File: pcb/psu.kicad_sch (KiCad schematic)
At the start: 35 parts

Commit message: add footprints
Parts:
- C201: renamed from C?; footprint (none) -> fpga:BGA256C100P16X16_1700X1700X155
- C202, C204, C205, C206, C207, C208, C209, C210, C211, C212, C213, C214, C215, C216, C217, C218, C219: renamed from C?; footprint (none) -> Capacitor_SMD:C_0805_2012Metric_Pad1.18x1.45mm_HandSolder
- C203: renamed from C?; footprint (none) -> Capacitor_SMD:C_1210_3225Metric_Pad1.33x2.70mm_HandSolder
- JP201, JP202, JP203: renamed from JP?; footprint (none) -> Jumper:SolderJumper-3_P1.3mm_Open_Pad1.0x1.5mm_NumberLabels
- L201, L202, L203: renamed from L?; footprint (none) -> Inductor_SMD:L_1210_3225Metric_Pad1.42x2.65mm_HandSolder
- R201, R202, R203, R204, R205, R206, R207, R208: renamed from R?; footprint (none) -> Resistor_SMD:R_0805_2012Metric_Pad1.20x1.40mm_HandSolder
- gave numbers to parts that had none: 2

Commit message: start layout
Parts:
- C201: footprint fpga:BGA256C100P16X16_1700X1700X155 -> Capacitor_SMD:C_0805_2012Metric_Pad1.18x1.45mm_HandSolder
- U201: footprint PWP14_2P31X2P46 -> TPS54325:TPS54325PWPR
- U202: footprint PWP16_2P31X2P46 -> TPS54294:TPS54294PWP
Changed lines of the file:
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@@
     (pin "2")
+  )
+  (symbol (lib_id "power:+1V8") (at 16.51 134.62 0) (unit 1)
+    (in_bom yes) (on_board yes) (fields_autoplaced)
+    (property "Reference" "#PWR0104" (id 0) (at 16.51 138.43 0)
+      (effects (font (size 1.27 1.27)) hide)
+    )
+    (property "Value" "+1V8" (id 1) (at 16.51 129.54 0))
+    (property "Footprint" "" (id 2) (at 16.51 134.62 0)
+      (effects (font (size 1.27 1.27)) hide)
+    )
+    (property "Datasheet" "" (id 3) (at 16.51 134.62 0)
+      (effects (font (size 1.27 1.27)) hide)
+    )
+    (pin "1")
   )
   (symbol (lib_id "Device:R") (at 195.58 146.05 0) (unit 1)
@@
       (effects (font (size 1.524 1.524)))
     )
-    (property "Footprint" "PWP16_2P31X2P46" (id 2) (at 154.94 115.824 0)
+    (property "Footprint" "TPS54294:TPS54294PWP" (id 2) (at 154.94 115.824 0)
       (effects (font (size 1.524 1.524)) hide)
     )
@@
     (pin "2")
   )
-  (symbol (lib_id "power:+1V8") (at 16.51 134.62 0) (unit 1)
-    (in_bom yes) (on_board yes) (fields_autoplaced)
-    (property "Reference" "#PWR0201" (id 0) (at 16.51 138.43 0)
-      (effects (font (size 1.27 1.27)) hide)
-    )
-    (property "Value" "+1V8" (id 1) (at 16.51 129.54 0))
-    (property "Footprint" "" (id 2) (at 16.51 134.62 0)
-      (effects (font (size 1.27 1.27)) hide)
-    )
-    (property "Datasheet" "" (id 3) (at 16.51 134.62 0)
-      (effects (font (size 1.27 1.27)) hide)
-    )
-    (pin "1")
-  )
   (symbol (lib_id "pspice:INDUCTOR") (at 71.12 134.62 0) (unit 1)
     (in_bom yes) (on_board yes)
@@
       (effects (font (size 1.524 1.524)))
     )
-    (property "Footprint" "PWP14_2P31X2P46" (id 2) (at 138.43 44.704 0)
+    (property "Footprint" "TPS54325:TPS54325PWPR" (id 2) (at 138.43 44.704 0)
       (effects (font (size 1.524 1.524)) hide)
     )
@@
       (effects (font (size 1.27 1.27)) (justify left))
     )
-    (property "Footprint" "fpga:BGA256C100P16X16_1700X1700X155" (id 2) (at 47.9552 147.32 0)
-      (effects (font (size 1.27 1.27)) hide)
-    )
+    (property "Footprint" "Capacitor_SMD:C_0805_2012Metric_Pad1.18x1.45mm_HandSolder" (id 2) (at 47.9552 147.32 0)
+      (effects (font (size 1.27 1.27)) hide)
+    )

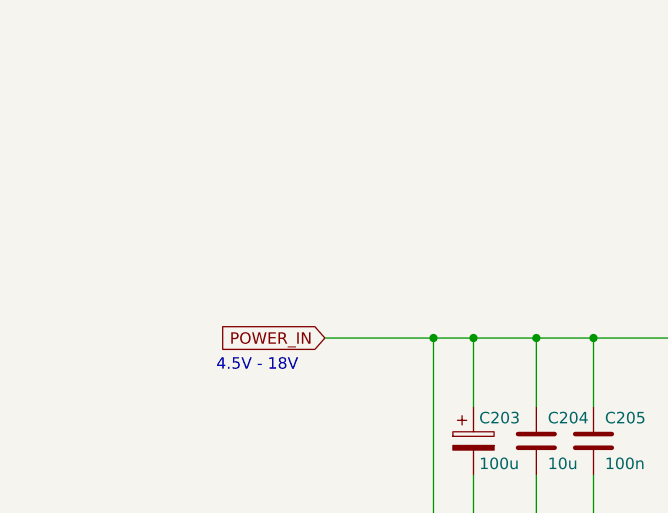
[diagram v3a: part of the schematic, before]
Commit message: add power input
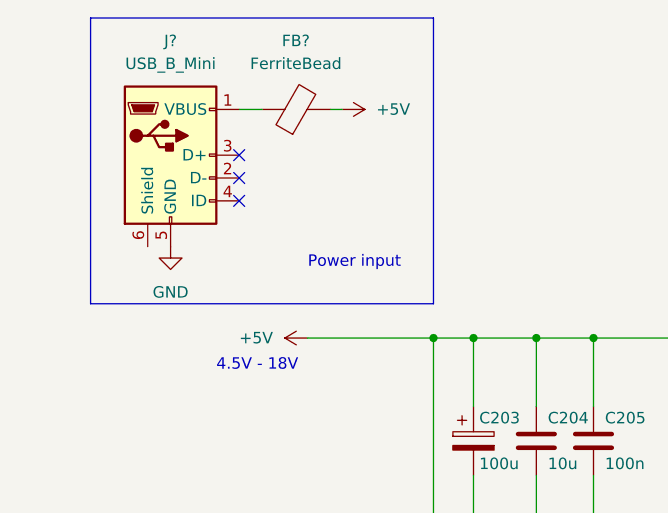
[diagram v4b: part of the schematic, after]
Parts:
- added FB?: FerriteBead, symbol Device:FerriteBead
- added J?: USB_B_Mini, symbol Connector:USB_B_Mini
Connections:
- net GND: now also J?.5 (GND)
- net POWER_IN renamed +5V
- net +5V: now also FB?.2
- new net: FB?.1, J?.1 (VBUS)
- no-connect marks 1 -> 4
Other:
- note added: "Power input"
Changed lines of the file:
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@@
   (junction (at 71.12 49.53) (diameter 0) (color 0 0 0 0)
   )
+  (no_connect (at 38.1 34.29))
   (no_connect (at 177.8 134.62))
+  (no_connect (at 38.1 31.75))
+  (no_connect (at 38.1 29.21))
   (wire (pts (xy 64.135 82.55) (xy 71.12 82.55))
     (stroke (width 0) (type default) (color 0 0 0 0))
@@
     (stroke (width 0) (type default) (color 0 0 0 0))
   )
+  (polyline (pts (xy 21.59 13.97) (xy 21.59 45.72))
+    (stroke (width 0) (type default) (color 0 0 0 0))
+  )
   (wire (pts (xy 180.34 132.08) (xy 180.34 153.67))
     (stroke (width 0) (type default) (color 0 0 0 0))
@@
     (stroke (width 0) (type default) (color 0 0 0 0))
   )
+  (polyline (pts (xy 21.59 13.97) (xy 59.69 13.97))
+    (stroke (width 0) (type default) (color 0 0 0 0))
+  )
   (wire (pts (xy 77.47 134.62) (xy 106.68 134.62))
     (stroke (width 0) (type default) (color 0 0 0 0))
@@
     (stroke (width 0) (type default) (color 0 0 0 0))
   )
+  (wire (pts (xy 38.1 24.13) (xy 40.64 24.13))
+    (stroke (width 0) (type default) (color 0 0 0 0))
+  )
   (wire (pts (xy 130.81 158.75) (xy 154.94 158.75))
     (stroke (width 0) (type default) (color 0 0 0 0))
@@
     (stroke (width 0) (type default) (color 0 0 0 0))
   )
-  (wire (pts (xy 47.625 49.53) (xy 59.69 49.53))
+  (wire (pts (xy 45.72 49.53) (xy 59.69 49.53))
     (stroke (width 0) (type default) (color 0 0 0 0))
   )
@@
     (stroke (width 0) (type default) (color 0 0 0 0))
   )
+  (polyline (pts (xy 59.69 13.97) (xy 59.69 45.72))
+    (stroke (width 0) (type default) (color 0 0 0 0))
+  )
+  (polyline (pts (xy 59.69 45.72) (xy 21.59 45.72))
+    (stroke (width 0) (type default) (color 0 0 0 0))
+  )
   (wire (pts (xy 106.68 133.35) (xy 106.68 134.62))
+    (stroke (width 0) (type default) (color 0 0 0 0))
+  )
+  (wire (pts (xy 48.26 24.13) (xy 49.53 24.13))
     (stroke (width 0) (type default) (color 0 0 0 0))
   )
@@
     (effects (font (size 1.27 1.27)) (justify left bottom))
   )
+  (text "Power input" (at 45.72 41.91 0)
+    (effects (font (size 1.27 1.27)) (justify left bottom))
+  )
   (text "1%\n" (at 92.71 73.66 90)
     (effects (font (size 1.27 1.27)) (justify left bottom))
@@
   (text "lp>2.8A, lrms>2.1A" (at 62.23 132.08 0)
     (effects (font (size 1.27 1.27)) (justify left bottom))
-  )
-  (global_label "POWER_IN" (shape input) (at 47.625 49.53 180) (fields_autoplaced)
-    (effects (font (size 1.27 1.27)) (justify right))
-    (property "Intersheet References" "${INTERSHEET_REFS}" (id 0) (at 35.8381 49.4506 0)
-      (effects (font (size 1.27 1.27)) (justify right) hide)
-    )
   )
   (symbol (lib_id "power:GND") (at 154.94 163.83 0) (unit 1)
@@
     (pin "2")
   )
+  (symbol (lib_id "Connector:USB_B_Mini") (at 30.48 29.21 0) (unit 1)
+    (in_bom yes) (on_board yes) (fields_autoplaced)
+    (property "Reference" "J?" (id 0) (at 30.48 16.51 0))
+    (property "Value" "USB_B_Mini" (id 1) (at 30.48 19.05 0))
+    (property "Footprint" "" (id 2) (at 34.29 30.48 0)
+      (effects (font (size 1.27 1.27)) hide)
+    )
+    (property "Datasheet" "~" (id 3) (at 34.29 30.48 0)
+      (effects (font (size 1.27 1.27)) hide)
+    )
+    (pin "1")
+    (pin "2")
+    (pin "3")
+    (pin "4")
+    (pin "5")
+    (pin "6")
+  )
   (symbol (lib_id "Device:R") (at 95.25 59.69 0) (unit 1)
     (in_bom yes) (on_board yes)
@@
     (pin "1")
     (pin "2")
+  )
+  (symbol (lib_id "power:GND") (at 30.48 39.37 0) (mirror y) (unit 1)
+    (in_bom yes) (on_board yes) (fields_autoplaced)
+    (property "Reference" "#PWR?" (id 0) (at 30.48 45.72 0)
+      (effects (font (size 1.27 1.27)) hide)
+    )
+    (property "Value" "GND" (id 1) (at 30.48 44.45 0))
+    (property "Footprint" "" (id 2) (at 30.48 39.37 0)
+      (effects (font (size 1.27 1.27)) hide)
+    )
+    (property "Datasheet" "" (id 3) (at 30.48 39.37 0)
+      (effects (font (size 1.27 1.27)) hide)
+    )
+    (pin "1")
   )
   (symbol (lib_id "Device:C") (at 193.04 129.54 0) (unit 1)
@@
     (pin "2")
   )
+  (symbol (lib_id "power:+5V") (at 49.53 24.13 270) (unit 1)
+    (in_bom yes) (on_board yes) (fields_autoplaced)
+    (property "Reference" "#PWR?" (id 0) (at 45.72 24.13 0)
+      (effects (font (size 1.27 1.27)) hide)
+    )
+    (property "Value" "+5V" (id 1) (at 53.34 24.1299 90)
+      (effects (font (size 1.27 1.27)) (justify left))
+    )
+    (property "Footprint" "" (id 2) (at 49.53 24.13 0)
+      (effects (font (size 1.27 1.27)) hide)
+    )
+    (property "Datasheet" "" (id 3) (at 49.53 24.13 0)
+      (effects (font (size 1.27 1.27)) hide)
+    )
+    (pin "1")
+  )
   (symbol (lib_id "Device:C") (at 214.63 124.46 0) (unit 1)
     (in_bom yes) (on_board yes) (fields_autoplaced)
@@
     )
     (property "Datasheet" "~" (id 3) (at 265.43 134.62 0)
+      (effects (font (size 1.27 1.27)) hide)
+    )
+    (pin "1")
+    (pin "2")
+  )
+  (symbol (lib_id "Device:FerriteBead") (at 44.45 24.13 90) (unit 1)
+    (in_bom yes) (on_board yes) (fields_autoplaced)
+    (property "Reference" "FB?" (id 0) (at 44.3992 16.51 90))
+    (property "Value" "FerriteBead" (id 1) (at 44.3992 19.05 90))
+    (property "Footprint" "" (id 2) (at 44.45 25.908 90)
+      (effects (font (size 1.27 1.27)) hide)
+    )
+    (property "Datasheet" "~" (id 3) (at 44.45 24.13 0)
       (effects (font (size 1.27 1.27)) hide)
     )
@@
     (pin "2")
   )
+  (symbol (lib_id "power:+5V") (at 45.72 49.53 90) (unit 1)
+    (in_bom yes) (on_board yes)
+    (property "Reference" "#PWR?" (id 0) (at 49.53 49.53 0)
+      (effects (font (size 1.27 1.27)) hide)
+    )
+    (property "Value" "+5V" (id 1) (at 38.1 49.53 90)
+      (effects (font (size 1.27 1.27)) (justify right))
+    )
+    (property "Footprint" "" (id 2) (at 45.72 49.53 0)
+      (effects (font (size 1.27 1.27)) hide)
+    )
+    (property "Datasheet" "" (id 3) (at 45.72 49.53 0)
+      (effects (font (size 1.27 1.27)) hide)
+    )
+    (pin "1")
+  )
   (symbol (lib_id "Device:C") (at 71.12 60.96 0) (unit 1)

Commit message: add footprint to usb
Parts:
- J?: footprint (none) -> usb:USB2066-05-RBHM-15-STB-00-00-A
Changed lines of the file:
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@@
   (no_connect (at 38.1 34.29))
   (no_connect (at 177.8 134.62))
+  (no_connect (at 38.1 29.21))
   (no_connect (at 38.1 31.75))
-  (no_connect (at 38.1 29.21))
   (wire (pts (xy 64.135 82.55) (xy 71.12 82.55))
     (stroke (width 0) (type default) (color 0 0 0 0))
@@
     (property "Reference" "J?" (id 0) (at 30.48 16.51 0))
     (property "Value" "USB_B_Mini" (id 1) (at 30.48 19.05 0))
-    (property "Footprint" "" (id 2) (at 34.29 30.48 0)
-      (effects (font (size 1.27 1.27)) hide)
-    )
+    (property "Footprint" "usb:USB2066-05-RBHM-15-STB-00-00-A" (id 2) (at 34.29 30.48 0)
+      (effects (font (size 1.27 1.27)) hide)
+    )

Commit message: change footprint of debug_connector
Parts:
- J201: renamed from J?; footprint usb:USB2066-05-RBHM-15-STB-00-00-A -> (none)
- gave numbers to parts that had none: 1
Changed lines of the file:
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@@
   (no_connect (at 38.1 34.29))
   (no_connect (at 177.8 134.62))
+  (no_connect (at 38.1 31.75))
   (no_connect (at 38.1 29.21))
-  (no_connect (at 38.1 31.75))
   (wire (pts (xy 64.135 82.55) (xy 71.12 82.55))
     (stroke (width 0) (type default) (color 0 0 0 0))
@@
   (symbol (lib_id "Connector:USB_B_Mini") (at 30.48 29.21 0) (unit 1)
     (in_bom yes) (on_board yes) (fields_autoplaced)
-    (property "Reference" "J?" (id 0) (at 30.48 16.51 0))
+    (property "Reference" "J201" (id 0) (at 30.48 16.51 0))
     (property "Value" "USB_B_Mini" (id 1) (at 30.48 19.05 0))
-    (property "Footprint" "usb:USB2066-05-RBHM-15-STB-00-00-A" (id 2) (at 34.29 30.48 0)
+    (property "Footprint" "" (id 2) (at 34.29 30.48 0)
       (effects (font (size 1.27 1.27)) hide)
     )
@@
   (symbol (lib_id "power:GND") (at 30.48 39.37 0) (mirror y) (unit 1)
     (in_bom yes) (on_board yes) (fields_autoplaced)
-    (property "Reference" "#PWR?" (id 0) (at 30.48 45.72 0)
+    (property "Reference" "#PWR0113" (id 0) (at 30.48 45.72 0)
       (effects (font (size 1.27 1.27)) hide)
     )
@@
   (symbol (lib_id "power:+5V") (at 49.53 24.13 270) (unit 1)
     (in_bom yes) (on_board yes) (fields_autoplaced)
-    (property "Reference" "#PWR?" (id 0) (at 45.72 24.13 0)
+    (property "Reference" "#PWR0112" (id 0) (at 45.72 24.13 0)
       (effects (font (size 1.27 1.27)) hide)
     )
@@
   (symbol (lib_id "Device:FerriteBead") (at 44.45 24.13 90) (unit 1)
     (in_bom yes) (on_board yes) (fields_autoplaced)
-    (property "Reference" "FB?" (id 0) (at 44.3992 16.51 90))
+    (property "Reference" "FB201" (id 0) (at 44.3992 16.51 90))
     (property "Value" "FerriteBead" (id 1) (at 44.3992 19.05 90))
     (property "Footprint" "" (id 2) (at 44.45 25.908 90)
@@
   (symbol (lib_id "power:+5V") (at 45.72 49.53 90) (unit 1)
     (in_bom yes) (on_board yes)
-    (property "Reference" "#PWR?" (id 0) (at 49.53 49.53 0)
-      (effects (font (size 1.27 1.27)) hide)
-    )
+    (property "Reference" "#PWR0111" (id 0) (at 49.53 49.53 0)
+      (effects (font (size 1.27 1.27)) hide)
+    )

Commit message: assign the last footprints
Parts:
- removed FB201: FerriteBead, symbol Device:FerriteBead
- J201: footprint (none) -> usb:USB2066-05-RBHM-15-STB-00-00-A
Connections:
- net +5V: now also J201.1 (VBUS)
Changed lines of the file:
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@@
-    (stroke (width 0) (type default) (color 0 0 0 0))
-  )
-  (wire (pts (xy 38.1 24.13) (xy 40.64 24.13))
     (stroke (width 0) (type default) (color 0 0 0 0))
   )
@@
   )
   (wire (pts (xy 106.68 133.35) (xy 106.68 134.62))
-    (stroke (width 0) (type default) (color 0 0 0 0))
-  )
-  (wire (pts (xy 48.26 24.13) (xy 49.53 24.13))
     (stroke (width 0) (type default) (color 0 0 0 0))
   )
@@
     (property "Reference" "J201" (id 0) (at 30.48 16.51 0))
     (property "Value" "USB_B_Mini" (id 1) (at 30.48 19.05 0))
-    (property "Footprint" "" (id 2) (at 34.29 30.48 0)
-      (effects (font (size 1.27 1.27)) hide)
-    )
+    (property "Footprint" "usb:USB2066-05-RBHM-15-STB-00-00-A" (id 2) (at 34.29 30.48 0))
     (property "Datasheet" "~" (id 3) (at 34.29 30.48 0)
       (effects (font (size 1.27 1.27)) hide)
@@
     (pin "2")
   )
-  (symbol (lib_id "power:+5V") (at 49.53 24.13 270) (unit 1)
-    (in_bom yes) (on_board yes) (fields_autoplaced)
-    (property "Reference" "#PWR0112" (id 0) (at 45.72 24.13 0)
-      (effects (font (size 1.27 1.27)) hide)
-    )
-    (property "Value" "+5V" (id 1) (at 53.34 24.1299 90)
-      (effects (font (size 1.27 1.27)) (justify left))
-    )
-    (property "Footprint" "" (id 2) (at 49.53 24.13 0)
-      (effects (font (size 1.27 1.27)) hide)
-    )
-    (property "Datasheet" "" (id 3) (at 49.53 24.13 0)
+  (symbol (lib_id "power:+5V") (at 38.1 24.13 270) (unit 1)
+    (in_bom yes) (on_board yes) (fields_autoplaced)
+    (property "Reference" "#PWR0112" (id 0) (at 34.29 24.13 0)
+      (effects (font (size 1.27 1.27)) hide)
+    )
+    (property "Value" "+5V" (id 1) (at 41.91 24.1299 90)
+      (effects (font (size 1.27 1.27)) (justify left))
+    )
+    (property "Footprint" "" (id 2) (at 38.1 24.13 0)
+      (effects (font (size 1.27 1.27)) hide)
+    )
+    (property "Datasheet" "" (id 3) (at 38.1 24.13 0)
       (effects (font (size 1.27 1.27)) hide)
     )
@@
       (effects (font (size 1.27 1.27)) hide)
     )
-    (pin "1")
-    (pin "2")
-  )
-  (symbol (lib_id "Device:FerriteBead") (at 44.45 24.13 90) (unit 1)
-    (in_bom yes) (on_board yes) (fields_autoplaced)
-    (property "Reference" "FB201" (id 0) (at 44.3992 16.51 90))
-    (property "Value" "FerriteBead" (id 1) (at 44.3992 19.05 90))
-    (property "Footprint" "" (id 2) (at 44.45 25.908 90)
-      (effects (font (size 1.27 1.27)) hide)
-    )
-    (property "Datasheet" "~" (id 3) (at 44.45 24.13 0)
-      (effects (font (size 1.27 1.27)) hide)
-    )

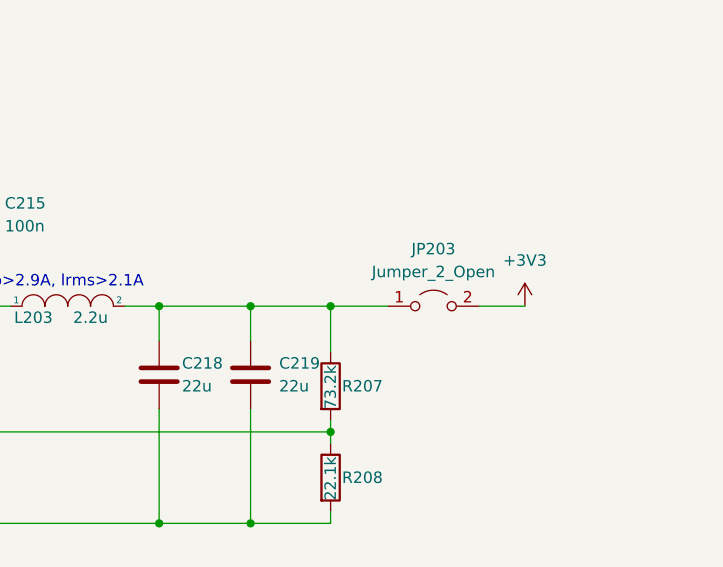
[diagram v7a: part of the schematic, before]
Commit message: psu wiring and power cables
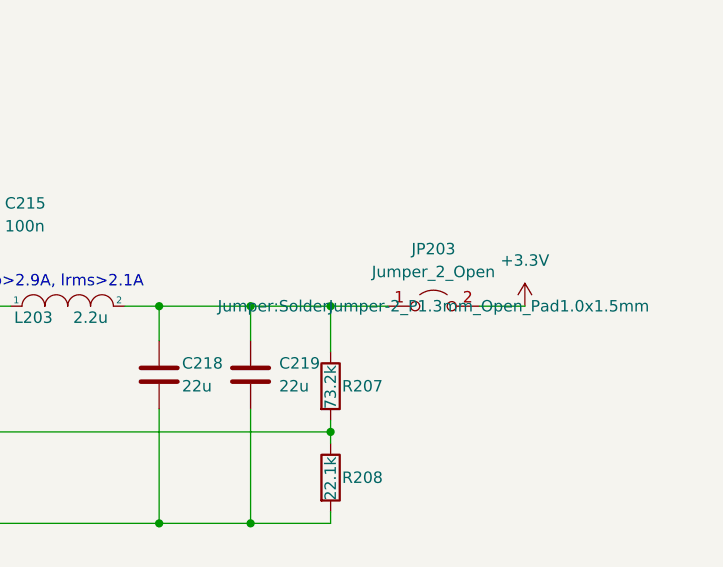
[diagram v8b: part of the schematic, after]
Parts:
- JP201, JP202, JP203: footprint Jumper:SolderJumper-3_P1.3mm_Open_Pad1.0x1.5mm_NumberLabels -> Jumper:SolderJumper-2_P1.3mm_Open_Pad1.0x1.5mm
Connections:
- net +3V3 renamed +3.3V
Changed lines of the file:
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@@
     (effects (font (size 1.27 1.27)) (justify left bottom))
+  )
+  (symbol (lib_id "power:+3.3V") (at 275.59 134.62 0) (unit 1)
+    (in_bom yes) (on_board yes) (fields_autoplaced)
+    (property "Reference" "#PWR0114" (id 0) (at 275.59 138.43 0)
+      (effects (font (size 1.27 1.27)) hide)
+    )
+    (property "Value" "+3.3V" (id 1) (at 275.59 129.54 0))
+    (property "Footprint" "" (id 2) (at 275.59 134.62 0)
+      (effects (font (size 1.27 1.27)) hide)
+    )
+    (property "Datasheet" "" (id 3) (at 275.59 134.62 0)
+      (effects (font (size 1.27 1.27)) hide)
+    )
+    (pin "1")
   )
   (symbol (lib_id "power:GND") (at 154.94 163.83 0) (unit 1)
@@
     (pin "2")
   )
-  (symbol (lib_id "power:+3V3") (at 275.59 134.62 0) (unit 1)
-    (in_bom yes) (on_board yes) (fields_autoplaced)
-    (property "Reference" "#PWR0205" (id 0) (at 275.59 138.43 0)
-      (effects (font (size 1.27 1.27)) hide)
-    )
-    (property "Value" "+3V3" (id 1) (at 275.59 129.54 0))
-    (property "Footprint" "" (id 2) (at 275.59 134.62 0)
-      (effects (font (size 1.27 1.27)) hide)
-    )
-    (property "Datasheet" "" (id 3) (at 275.59 134.62 0)
-      (effects (font (size 1.27 1.27)) hide)
-    )
-    (pin "1")
-  )
   (symbol (lib_id "Device:C") (at 234.95 142.24 0) (unit 1)
     (in_bom yes) (on_board yes)
@@
     (property "Reference" "JP201" (id 0) (at 26.67 128.27 0))
     (property "Value" "Jumper_2_Open" (id 1) (at 26.67 130.81 0))
-    (property "Footprint" "Jumper:SolderJumper-3_P1.3mm_Open_Pad1.0x1.5mm_NumberLabels" (id 2) (at 26.67 134.62 0)
+    (property "Footprint" "Jumper:SolderJumper-2_P1.3mm_Open_Pad1.0x1.5mm" (id 2) (at 26.67 134.62 0)
       (effects (font (size 1.27 1.27)) hide)
     )
@@
     (property "Reference" "JP202" (id 0) (at 243.84 43.18 0))
     (property "Value" "Jumper_2_Open" (id 1) (at 243.84 45.72 0))
-    (property "Footprint" "Jumper:SolderJumper-3_P1.3mm_Open_Pad1.0x1.5mm_NumberLabels" (id 2) (at 243.84 49.53 0)
+    (property "Footprint" "Jumper:SolderJumper-2_P1.3mm_Open_Pad1.0x1.5mm" (id 2) (at 243.84 49.53 0)
       (effects (font (size 1.27 1.27)) hide)
     )
@@
     (property "Reference" "JP203" (id 0) (at 265.43 128.27 0))
     (property "Value" "Jumper_2_Open" (id 1) (at 265.43 130.81 0))
-    (property "Footprint" "Jumper:SolderJumper-3_P1.3mm_Open_Pad1.0x1.5mm_NumberLabels" (id 2) (at 265.43 134.62 0)
-      (effects (font (size 1.27 1.27)) hide)
-    )
+    (property "Footprint" "Jumper:SolderJumper-2_P1.3mm_Open_Pad1.0x1.5mm" (id 2) (at 265.43 134.62 0))
     (property "Datasheet" "~" (id 3) (at 265.43 134.62 0)
       (effects (font (size 1.27 1.27)) hide)
